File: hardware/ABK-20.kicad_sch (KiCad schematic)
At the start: 52 parts, among them J1 CONN_01X04, J2 CONN_01X04, J3 CONN_02X03, J4 Con_3-5V, J5 USB_C_6P, J6 Sync_Jumper, SW1 SW_SPST, SW2 SW_Push_LED, SW3 SW_SPDT_MSM, SW4 SW_Push, U1 ATTINY85-20SU, U2 PAM8002, U3 7805

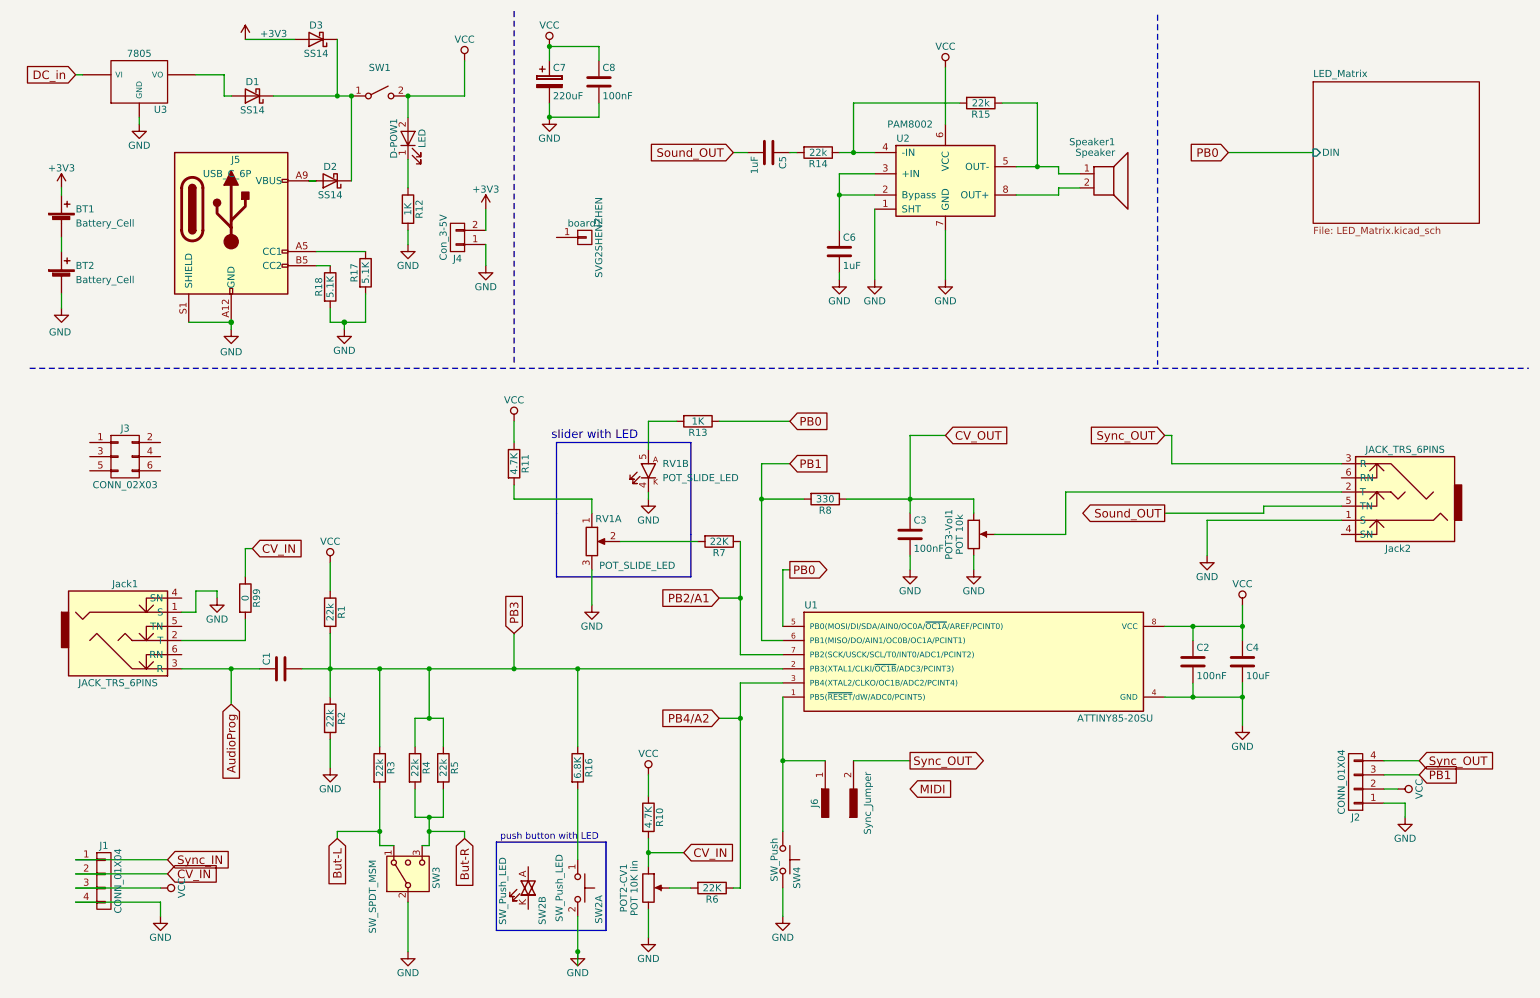
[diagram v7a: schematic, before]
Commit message: Sync schematic and PCB: restore BT1/BT2/J3 and fix Jack1/Jack2 pin 6
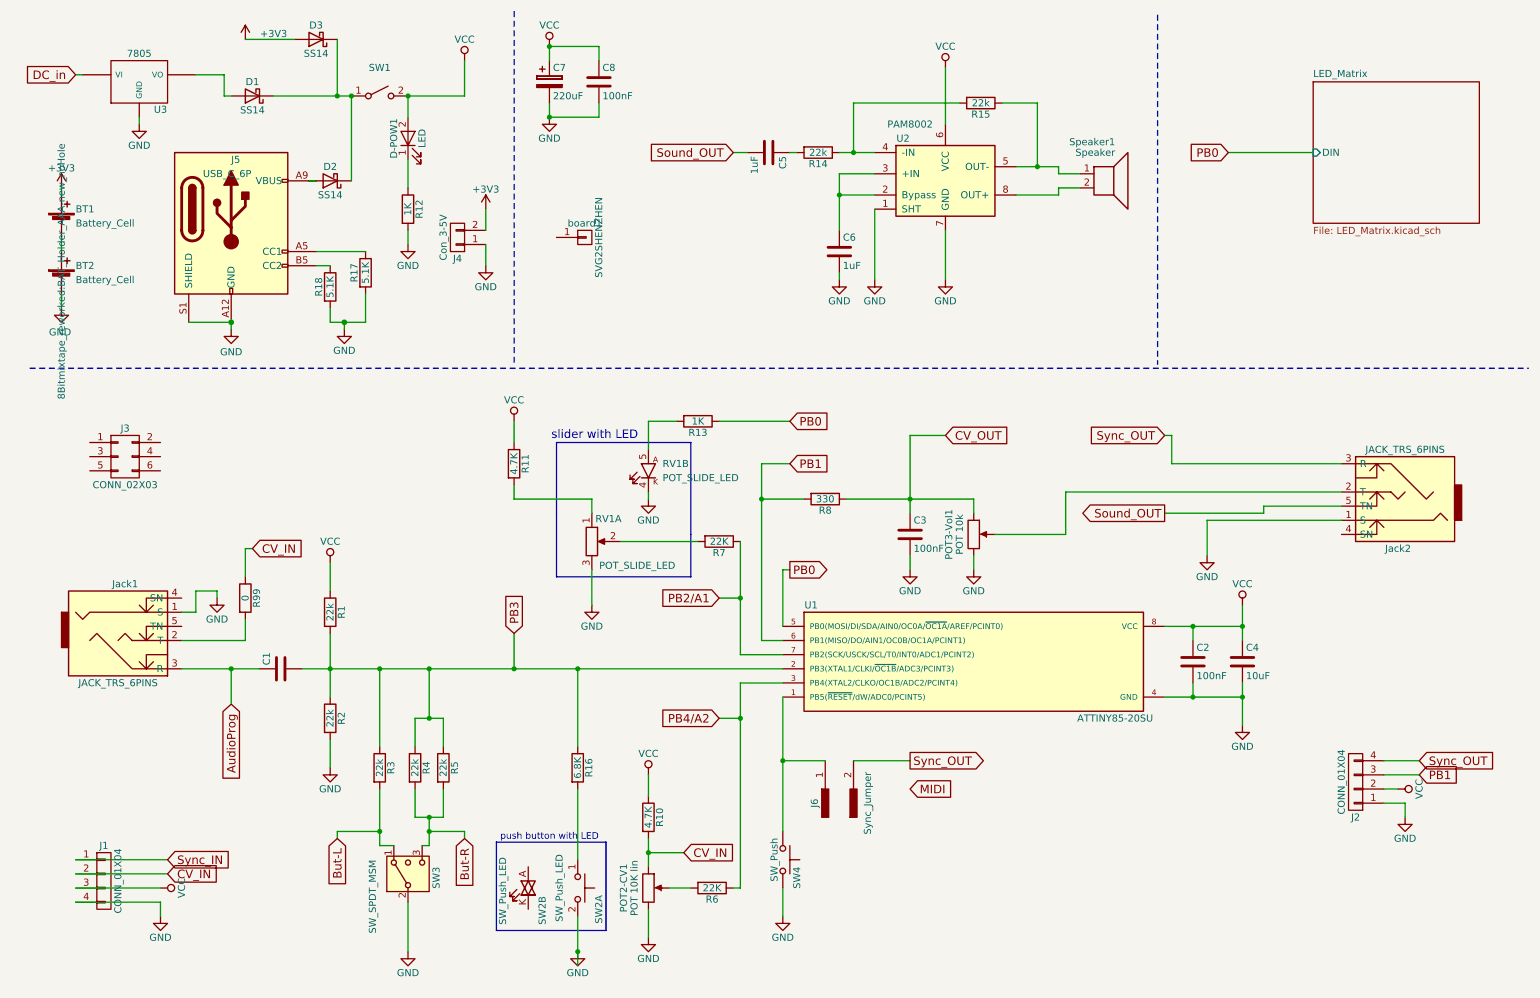
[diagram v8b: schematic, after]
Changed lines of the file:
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@@
 		(pin "2"
 		)
-		(pin "6"
-		)
 		(pin "3"
 		)
@@
 		(pin "2"
 		)
-		(pin "6"
-		)
 		(pin "3"
 		)
@@
 					(size 1.27 1.27)
 				)
-				(hide yes)
 			)
 		)
